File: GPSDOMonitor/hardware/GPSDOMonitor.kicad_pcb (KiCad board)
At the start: 2 copper layers, 150 x 60 mm, 35 parts, among them J1 F31S-1A7L1-11050, Q1 MMBT3904LT1G, U1 TPS563231DRLR, U2 MCP16301T-I_CHY, U3 PIC18LF2550-ISO, U4 SN74HC595BRWNR, U5 SN74HC595BRWNR, X1 ABM8W-20.0000MHZ-4-K1Z-T3

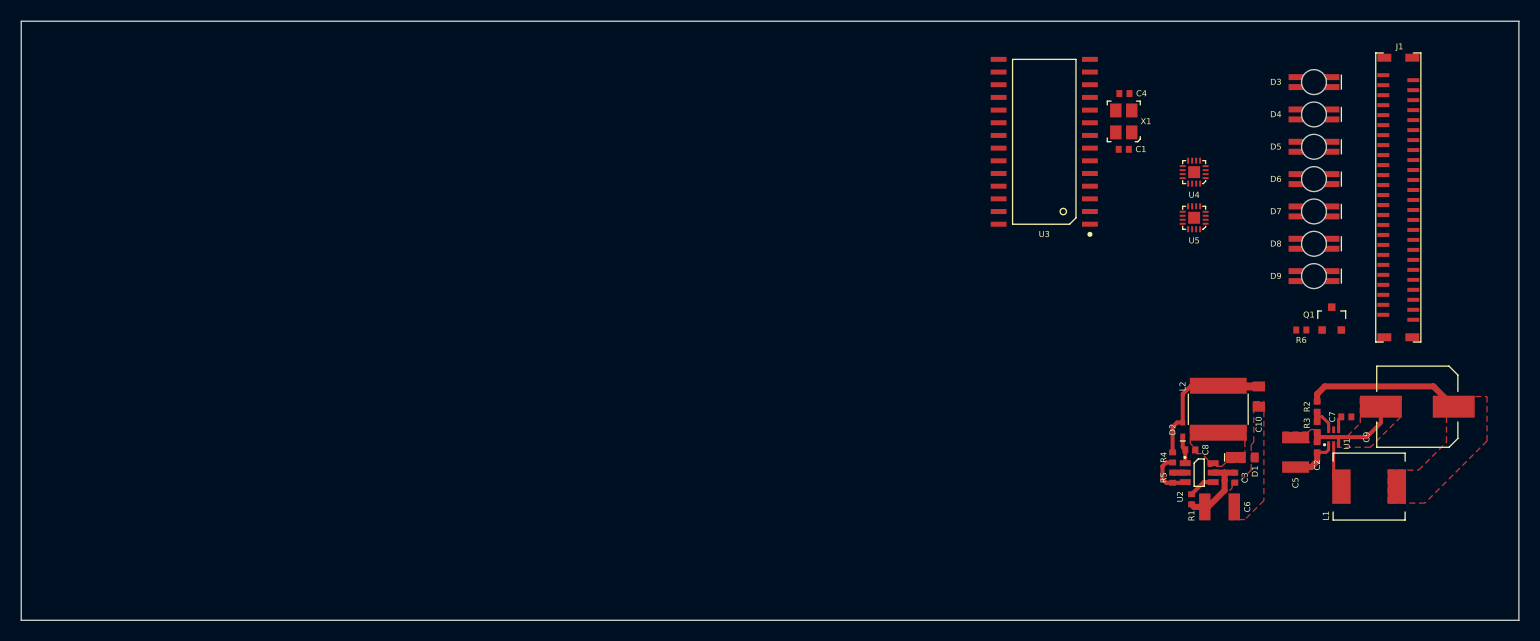
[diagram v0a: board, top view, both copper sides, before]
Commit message: Route majority of the current board
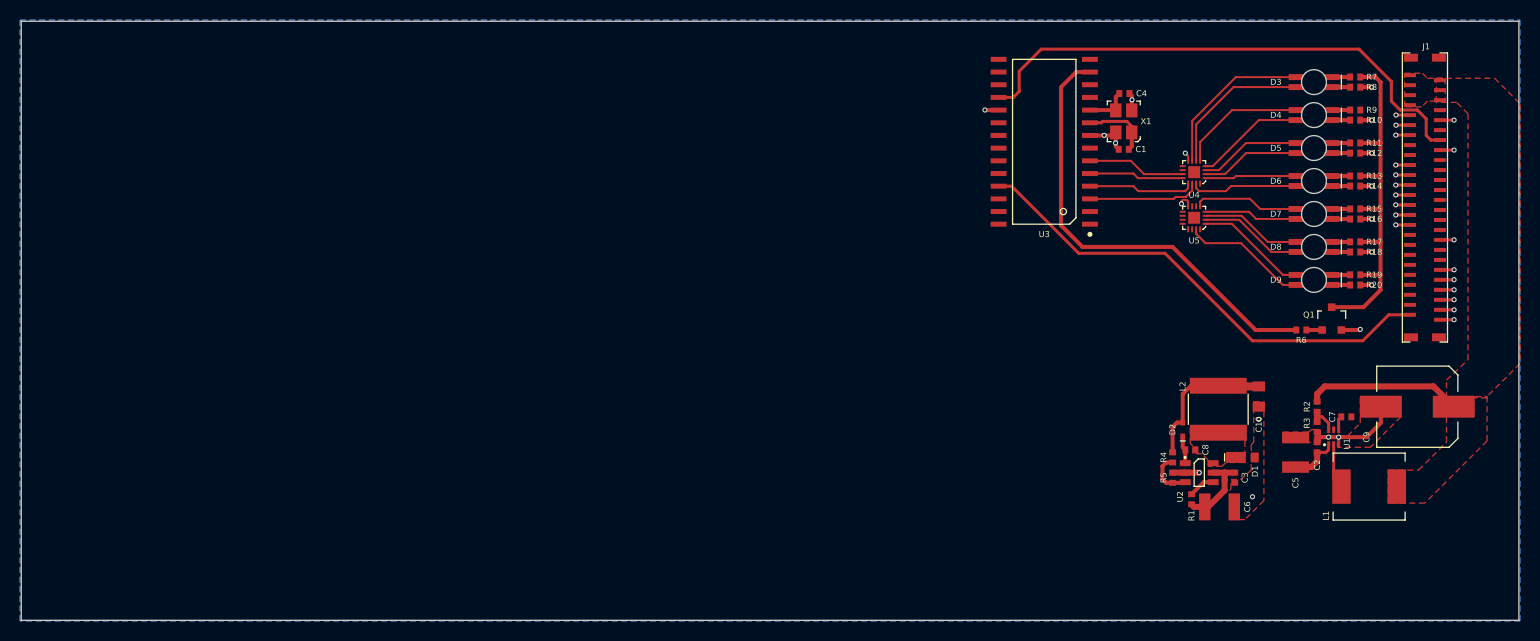
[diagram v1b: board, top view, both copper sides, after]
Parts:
- added R10: CRGCQ0402F68R, Resistor:R_0402_1005Metric, F.Cu at (177.2, 48.0)
- added R11: CRGCQ0402F68R, Resistor:R_0402_1005Metric, F.Cu at (177.2, 50.3)
- added R12: CRGCQ0402F68R, Resistor:R_0402_1005Metric, F.Cu at (177.2, 51.3)
- added R13: CRGCQ0402F68R, Resistor:R_0402_1005Metric, F.Cu at (177.2, 53.6)
- added R14: CRGCQ0402F68R, Resistor:R_0402_1005Metric, F.Cu at (177.2, 54.6)
- added R15: CRGCQ0402F68R, Resistor:R_0402_1005Metric, F.Cu at (177.2, 56.9)
- added R16: CRGCQ0402F68R, Resistor:R_0402_1005Metric, F.Cu at (177.2, 57.9)
- added R17: CRGCQ0402F68R, Resistor:R_0402_1005Metric, F.Cu at (177.2, 60.2)
- added R18: CRGCQ0402F68R, Resistor:R_0402_1005Metric, F.Cu at (177.2, 61.2)
- added R19: CRGCQ0402F68R, Resistor:R_0402_1005Metric, F.Cu at (177.2, 63.5)
- added R20: CRGCQ0402F68R, Resistor:R_0402_1005Metric, F.Cu at (177.2, 64.5)
- added R7: CRGCQ0402F68R, Resistor:R_0402_1005Metric, F.Cu at (177.2, 43.7)
- added R8: CRGCQ0402F68R, Resistor:R_0402_1005Metric, F.Cu at (177.2, 44.7)
- added R9: CRGCQ0402F68R, Resistor:R_0402_1005Metric, F.Cu at (177.2, 47.0)
- moved J1 2.67 mm to (187.1, 55.8)
- moved D9 0.38 mm to (173.0, 64.0)
- moved D8 0.32 mm to (173.0, 60.7)
- moved D7 0.25 mm to (173.0, 57.4)
- moved D6 0.19 mm to (173.0, 54.1)
- moved D5 0.13 mm to (173.0, 50.8)
- moved D4 0.06 mm to (173.0, 47.5)
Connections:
- D4 pad 4: Net-(D3-Pad4) -> Net-(D4-Pad4)
- D5 pad 4: Net-(D3-Pad4) -> Net-(D5-Pad4)
- D6 pad 4: Net-(D3-Pad4) -> Net-(D6-Pad4)
- D7 pad 4: Net-(D3-Pad4) -> Net-(D7-Pad4)
- D8 pad 4: Net-(D3-Pad4) -> Net-(D8-Pad4)
- D9 pad 4: Net-(D3-Pad4) -> Net-(D9-Pad4)
- Q1 pad 3: Net-(D3-Pad4) -> Net-(Q1-Pad3)
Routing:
- net UART3_TxD: track 0.00 -> 53.3 mm
- net UART4_TX: track 0.00 -> 48.7 mm
- net GND: track 11.7 -> 60.2 mm, vias 0 -> 38
- net /LED_PWM: track 0.00 -> 45.3 mm
- net Net-(Q1-Pad3): track 0.00 -> 38.8 mm
- net Net-(D3-Pad3): track 0.00 -> 16.2 mm
- net Net-(D3-Pad2): track 0.00 -> 15.2 mm
- net Net-(D4-Pad3): track 0.00 -> 12.8 mm
- net Net-(D9-Pad2): track 0.00 -> 12.6 mm
- net /SER: track 0.00 -> 11.3 mm
- net Net-(D9-Pad3): track 0.00 -> 11.2 mm
- net Net-(D4-Pad2): track 0.00 -> 11.0 mm
- net Net-(D6-Pad2): track 0.00 -> 10.8 mm
- net /OE: track 0.00 -> 10.6 mm
- net Net-(D7-Pad3): track 0.00 -> 10.6 mm
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- added copper zone on B.Cu, net GND
